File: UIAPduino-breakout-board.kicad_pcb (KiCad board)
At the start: 2 copper layers, 5 parts, among them J1 Conn_01x20_Pin, J2 Conn_01x20_Socket

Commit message: reload
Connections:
- J1 pad 7: GND -> Net-(J1-Pin_7)
- J2 pad 7: GND -> Net-(J1-Pin_7)
- U2 pad 18: Net-(J1-Pin_9) -> Net-(J1-Pin_8)
- U2 pad 22: Net-(J1-Pin_8) -> Net-(J1-Pin_7)
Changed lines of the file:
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@@
 	(net 18 "Net-(U1-TX)")
 	(net 19 "Net-(U1-RX)")
+	(net 20 "Net-(J1-Pin_7)")
 	(footprint "akizuki:FT234X"
 		(layer "F.Cu")
@@
 			(layers "*.Cu" "*.Mask")
 			(remove_unused_layers no)
-			(net 3 "GND")
+			(net 20 "Net-(J1-Pin_7)")
 			(pinfunction "Pin_7")
 			(pintype "passive")
@@
 			(layers "*.Cu" "*.Paste" "*.Mask")
 			(remove_unused_layers no)
-			(net 7 "Net-(J1-Pin_9)")
+			(net 2 "Net-(J1-Pin_8)")
 			(pinfunction "0/A1")
 			(pintype "bidirectional")
@@
 			(layers "*.Cu" "*.Paste" "*.Mask")
 			(remove_unused_layers no)
-			(net 2 "Net-(J1-Pin_8)")
+			(net 20 "Net-(J1-Pin_7)")
 			(pinfunction "~{RESET}")
 			(pintype "power_in")
@@
 			(layers "*.Cu" "*.Mask")
 			(remove_unused_layers no)
-			(net 3 "GND")
+			(net 20 "Net-(J1-Pin_7)")
 			(pinfunction "Pin_7")
 			(pintype "passive")

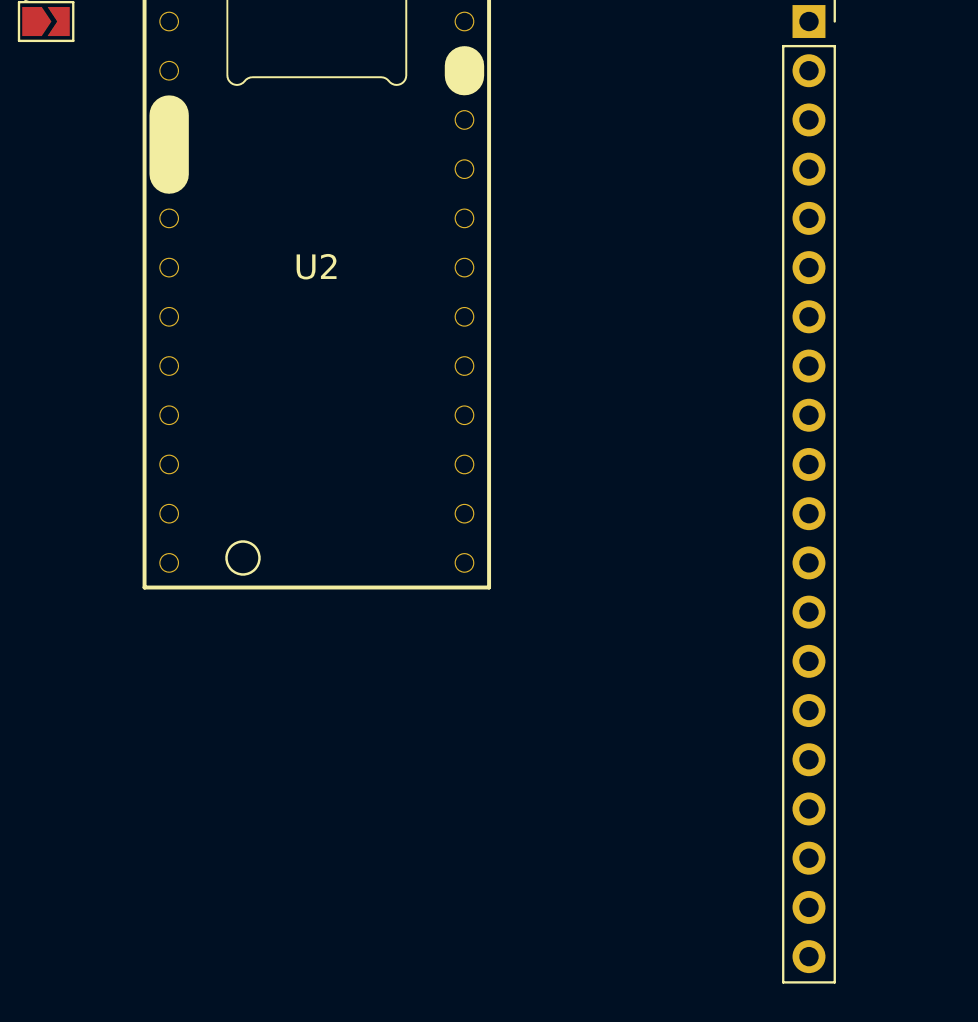
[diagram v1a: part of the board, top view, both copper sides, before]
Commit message: 信号線を配線
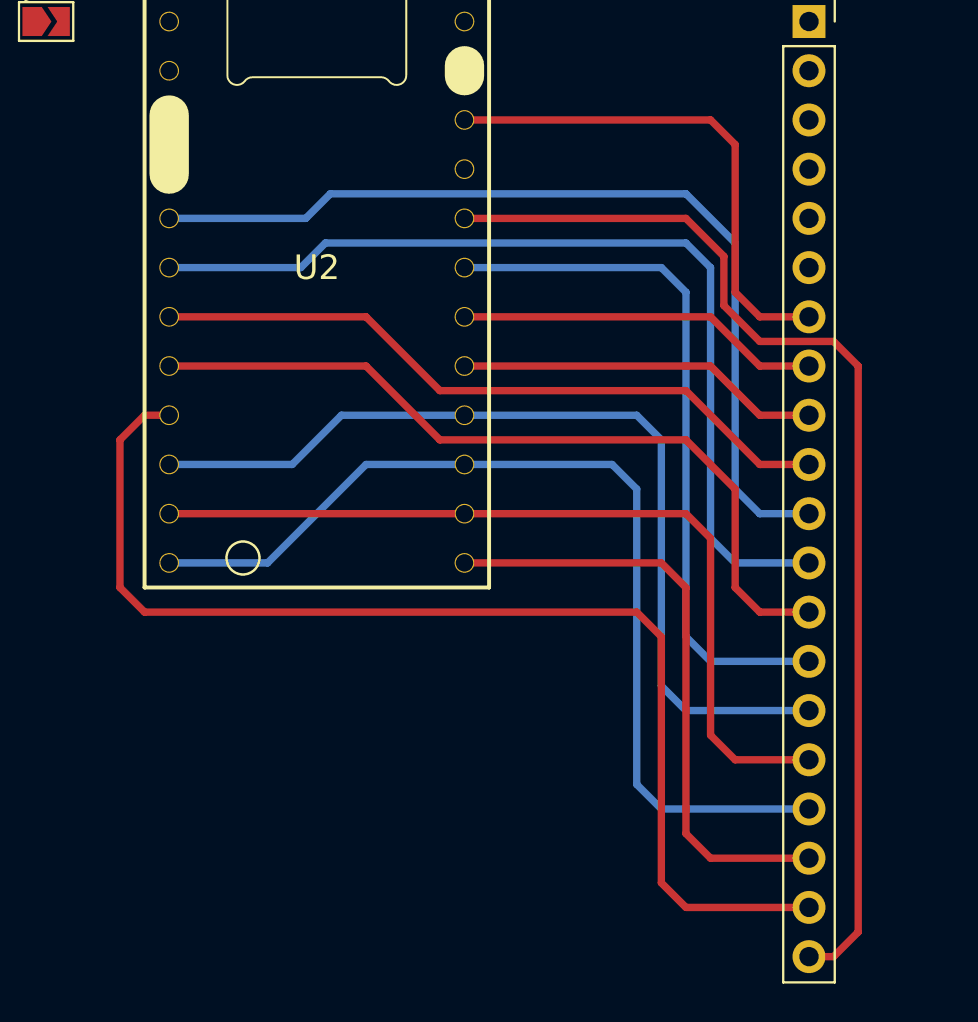
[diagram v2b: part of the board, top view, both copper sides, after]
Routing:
- net Net-(J1-Pin_19): track 0.00 -> 60.5 mm
- net Net-(J1-Pin_20): track 0.00 -> 57.2 mm
- net Net-(J1-Pin_17): track 0.00 -> 51.4 mm
- net Net-(J1-Pin_12): track 0.00 -> 48.6 mm
- net Net-(J1-Pin_15): track 0.00 -> 47.8 mm
- net Net-(J1-Pin_11): track 0.00 -> 47.8 mm
- net Net-(J1-Pin_16): track 0.00 -> 44.2 mm
- net Net-(J1-Pin_13): track 0.00 -> 41.3 mm
- net Net-(J1-Pin_14): track 0.00 -> 36.6 mm
- net Net-(J1-Pin_10): track 0.00 -> 36.2 mm
- net Net-(J1-Pin_18): track 0.00 -> 31.5 mm
- net Net-(J1-Pin_7): track 0.00 -> 26.5 mm
- net Net-(J1-Pin_8): track 0.00 -> 18.8 mm
- net Net-(J1-Pin_9): track 0.00 -> 18.8 mm

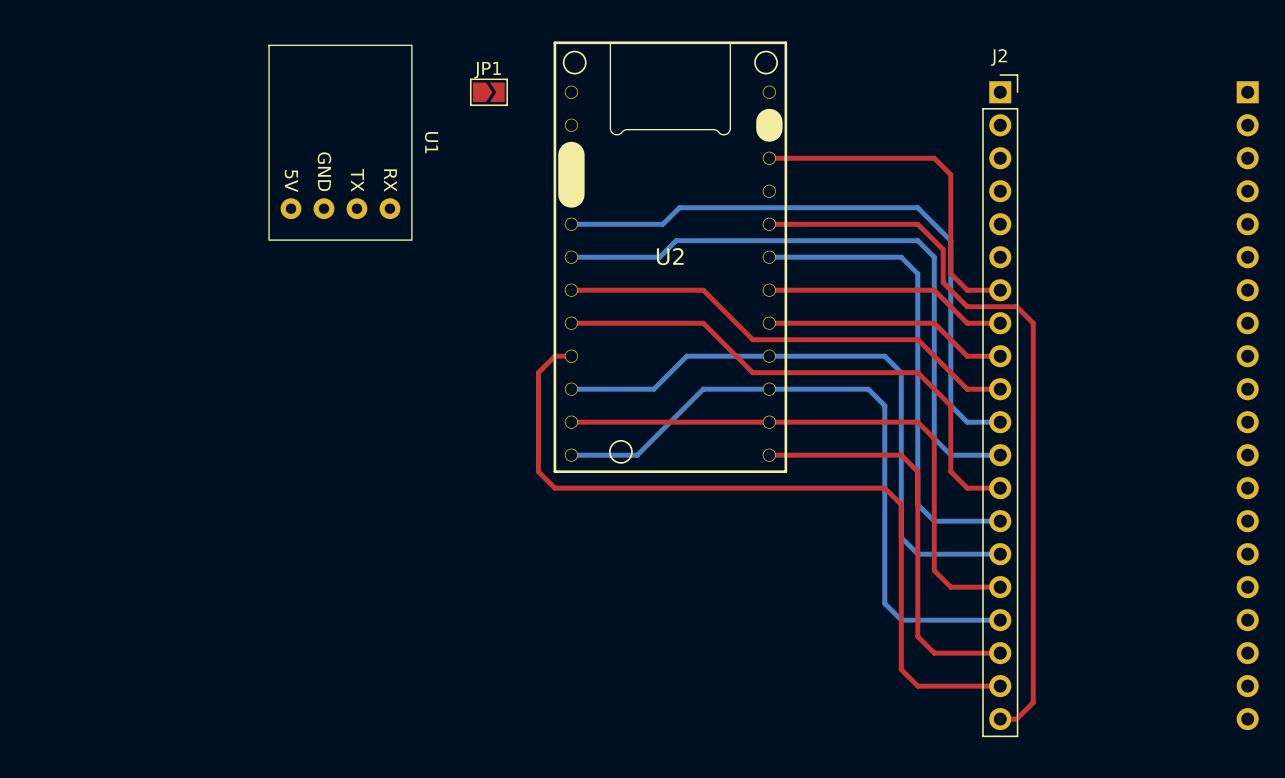
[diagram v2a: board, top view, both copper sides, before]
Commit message: 電源配置を変更
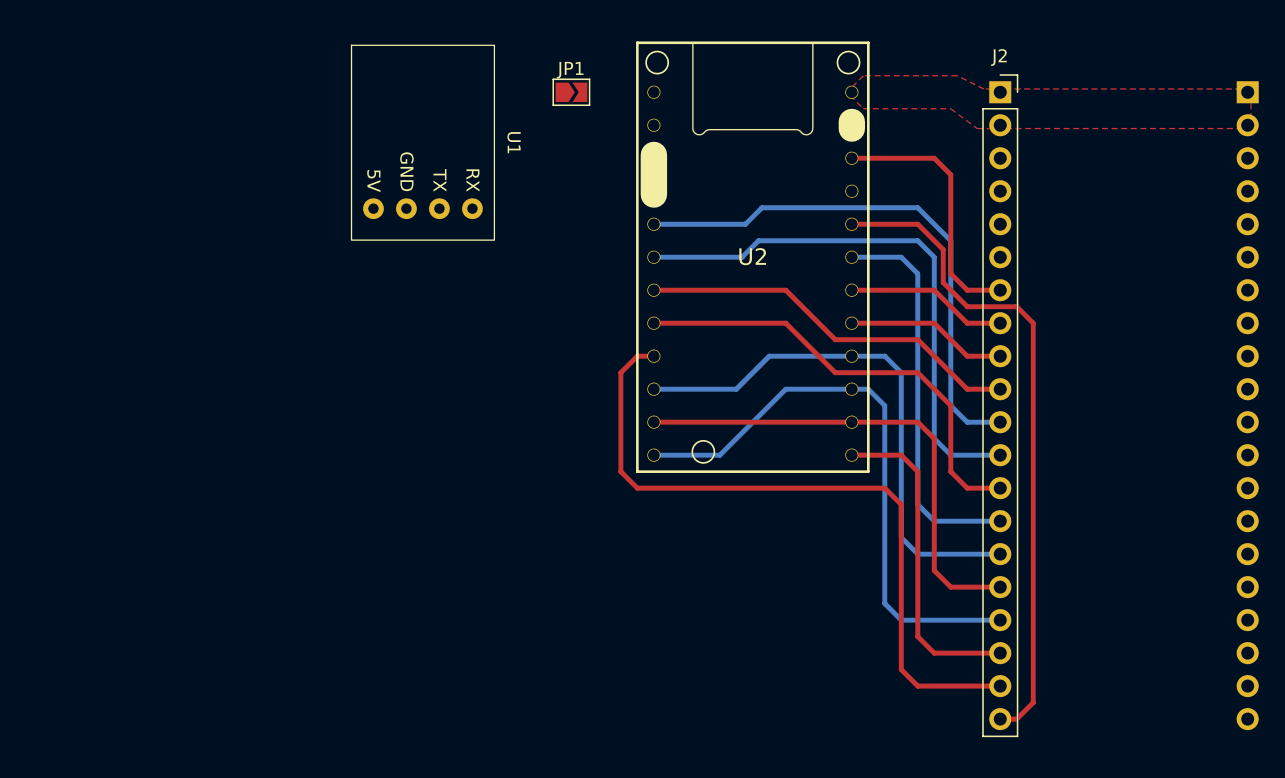
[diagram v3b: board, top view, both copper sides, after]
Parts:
- moved JP1 6.35 mm to (138.4, 67.3)
- moved U1 6.35 mm to (127.0, 63.6)
- moved U2 6.35 mm to (152.4, 80.0)
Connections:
- J1 pad 3: +3.3V -> GND
- J1 pad 4: +3.3V -> GND
- J1 pad 5: GND -> +3.3V
- J1 pad 6: GND -> +3.3V
- J2 pad 3: +3.3V -> GND
- J2 pad 4: +3.3V -> GND
- J2 pad 5: GND -> +3.3V
- J2 pad 6: GND -> +3.3V
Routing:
- net Net-(J1-Pin_19): track 60.5 -> 54.2 mm
- net Net-(J1-Pin_9): track 18.8 -> 12.5 mm
- net Net-(J1-Pin_8): track 18.8 -> 12.5 mm
- net Net-(J1-Pin_7): track 26.5 -> 20.1 mm
- net Net-(J1-Pin_20): track 57.2 -> 50.9 mm
- net Net-(J1-Pin_18): track 31.5 -> 25.2 mm
- net Net-(J1-Pin_14): track 36.6 -> 30.3 mm
- net Net-(J1-Pin_12): track 48.6 -> 42.2 mm
- net Net-(J1-Pin_16): track 44.2 -> 37.9 mm
- net Net-(J1-Pin_13): track 41.3 -> 34.9 mm
- net Net-(J1-Pin_11): track 47.8 -> 41.5 mm
- net Net-(J1-Pin_10): track 36.2 -> 29.8 mm
- net Net-(J1-Pin_17): track 51.4 -> 45.1 mm
- net Net-(J1-Pin_15): track 47.8 -> 41.5 mm
- added copper zone on F.Cu, net +5V

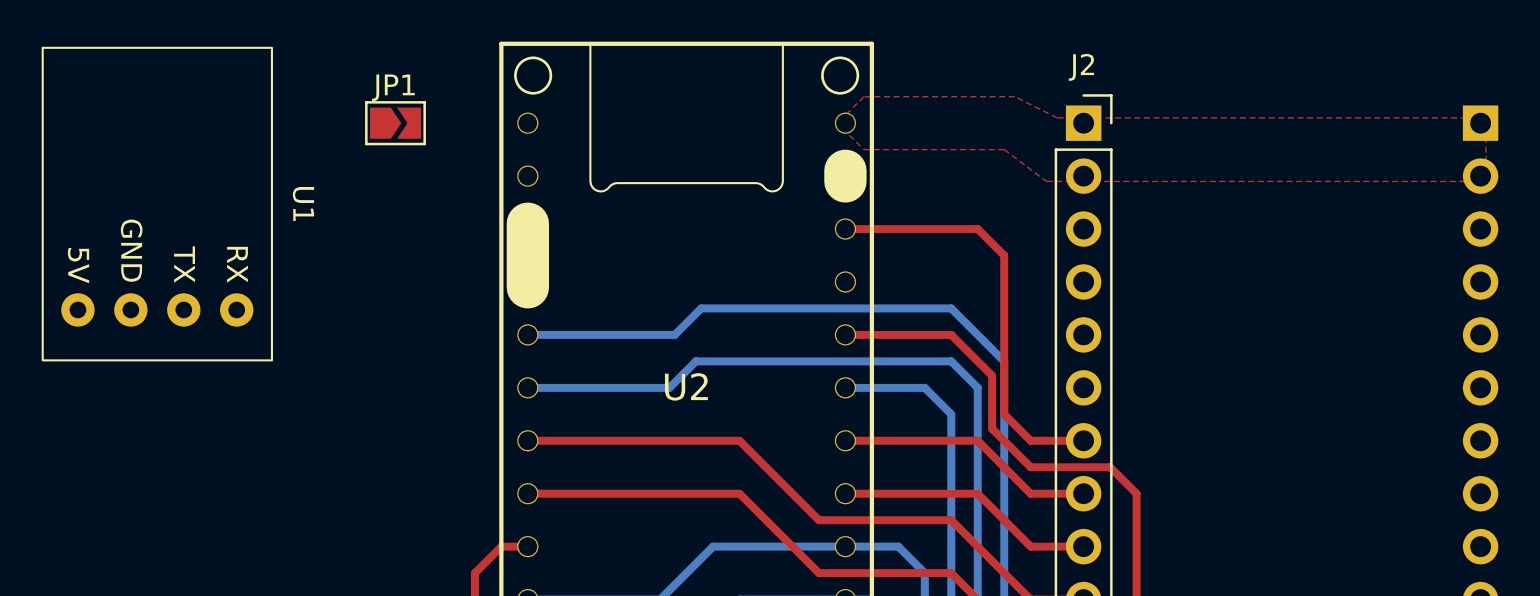
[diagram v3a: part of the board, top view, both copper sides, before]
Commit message: 配線をいい感じに
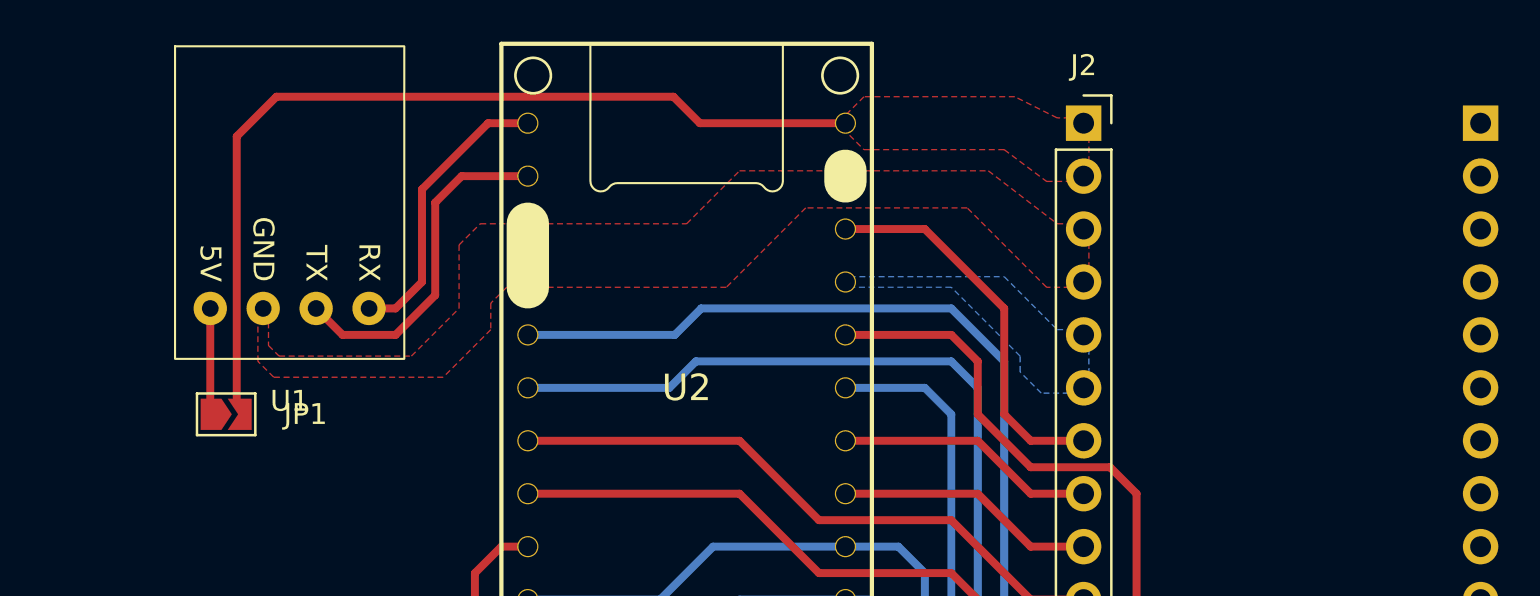
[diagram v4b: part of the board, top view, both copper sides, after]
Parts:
- moved JP1 16.2 mm to (130.3, 81.3)
- moved U1 6.35 mm to (133.3, 63.5)
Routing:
- net +5V: track 0.00 -> 43.7 mm
- net Net-(U1-TX): track 0.00 -> 16.4 mm
- net Net-(U1-RX): track 0.00 -> 13.9 mm
- net Net-(JP1-A): track 0.00 -> 5.08 mm
- net Net-(J1-Pin_7): track 20.1 -> 18.6 mm
- added copper zone on B.Cu, net +3.3V
- added copper zone on F.Cu, net GND
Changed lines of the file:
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@@
 	(footprint "akizuki:FT234X"
 		(layer "F.Cu")
-		(at 127 63.5725)
+		(at 133.35 63.5)
 		(property "Reference" "U1"
-			(at 6.985 7.62 -90)
+			(at 0 17.145 0)
 			(unlocked yes)
 			(layer "F.SilkS")
@@
 			(pinfunction "5V")
 			(pintype "power_out")
+			(thermal_bridge_angle 0)
 		)
 		(pad "2" thru_hole circle
@@
 			(pinfunction "GND")
 			(pintype "power_in")
+			(thermal_bridge_angle 0)
 		)
 		(pad "3" thru_hole circle
@@
 	(footprint "Jumper:SolderJumper-2_P1.3mm_Open_TrianglePad1.0x1.5mm"
 		(layer "F.Cu")
-		(at 138.43 67.31)
+		(at 130.302 81.28)
 		(descr "SMD Solder Jumper, 1x1.5mm Triangular Pads, 0.3mm gap, open")
 		(tags "solder jumper open")
 		(property "Reference" "JP1"
-			(at 0 -1.8 0)
+			(at 3.81 0 180)
 			(layer "F.SilkS")
 			(effects
@@
 		)
 		(property "Value" "Jumper_2_Open"
-			(at 0 1.9 0)
+			(at 0 1.9 360)
 			(layer "F.Fab")
 			(effects
@@
 			(pinfunction "GND")
 			(pintype "power_in")
+			(thermal_bridge_angle 0)
 		)
 		(pad "4" thru_hole circle
@@
 			(pinfunction "GND")
 			(pintype "power_in")
+			(thermal_bridge_angle 0)
 		)
 		(pad "5" thru_hole circle
@@
 			(pinfunction "3V3")
 			(pintype "power_in")
+			(thermal_bridge_angle 0)
 		)
 		(pad "22" thru_hole circle
@@
 			(pinfunction "GND")
 			(pintype "power_in")
+			(thermal_bridge_angle 0)
 		)
 		(pad "24" thru_hole circle
@@
 	)
 	(segment
+		(start 130.81 80.772)
+		(end 130.81 67.945)
+		(width 0.381)
+		(layer "F.Cu")
+		(net 1)
+	)
+	(segment
+		(start 153.035 67.31)
+		(end 160.02 67.31)
+		(width 0.381)
+		(layer "F.Cu")
+		(net 1)
+	)
+	(segment
+		(start 130.81 67.945)
+		(end 132.715 66.04)
+		(width 0.381)
+		(layer "F.Cu")
+		(net 1)
+	)
+	(segment
+		(start 131.064 81.026)
+		(end 130.81 80.772)
+		(width 0.381)
+		(layer "F.Cu")
+		(net 1)
+	)
+	(segment
+		(start 151.765 66.04)
+		(end 153.035 67.31)
+		(width 0.381)
+		(layer "F.Cu")
+		(net 1)
+	)
+	(segment
+		(start 132.715 66.04)
+		(end 151.765 66.04)
+		(width 0.381)
+		(layer "F.Cu")
+		(net 1)
+	)
+	(segment
 		(start 168.91 85.09)
 		(end 166.37 82.55)
@@
 	)
 	(segment
-		(start 172.72 83.82)
-		(end 173.99 85.09)
+		(start 166.37 78.74)
+		(end 166.37 81.28)
 		(width 0.381)
 		(layer "F.Cu")
@@
 	)
 	(segment
-		(start 167.059 81.969)
-		(end 168.91 83.82)
+		(start 165.1 77.47)
+		(end 166.37 78.74)
 		(width 0.381)
 		(layer "F.Cu")
@@
 	)
 	(segment
-		(start 165.1 77.47)
-		(end 160.02 77.47)
+		(start 173.99 114.3)
+		(end 172.72 115.57)
 		(width 0.381)
 		(layer "F.Cu")
@@
 	)
 	(segment
-		(start 173.99 85.09)
-		(end 173.99 114.3)
+		(start 172.72 83.82)
+		(end 173.99 85.09)
 		(width 0.381)
 		(layer "F.Cu")
@@
 	)
 	(segment
-		(start 167.059 79.429)
-		(end 167.059 81.969)
+		(start 166.37 81.28)
+		(end 168.91 83.82)
 		(width 0.381)
 		(layer "F.Cu")
@@
 	)
 	(segment
-		(start 165.1 77.47)
-		(end 167.059 79.429)
+		(start 172.72 115.57)
+		(end 171.45 115.57)
 		(width 0.381)
 		(layer "F.Cu")
@@
 	)
 	(segment
-		(start 173.99 114.3)
-		(end 172.72 115.57)
+		(start 168.91 83.82)
+		(end 172.72 83.82)
 		(width 0.381)
 		(layer "F.Cu")
@@
 	)
 	(segment
-		(start 172.72 115.57)
-		(end 171.45 115.57)
+		(start 160.02 77.47)
+		(end 165.1 77.47)
 		(width 0.381)
 		(layer "F.Cu")
@@
 	)
 	(segment
-		(start 168.91 83.82)
-		(end 172.72 83.82)
+		(start 173.99 85.09)
+		(end 173.99 114.3)
 		(width 0.381)
 		(layer "F.Cu")
@@
 	)
 	(segment
-		(start 166.37 72.39)
-		(end 160.02 72.39)
+		(start 129.54 81.28)
+		(end 129.54 76.2)
 		(width 0.381)
 		(layer "F.Cu")
-		(net 20)
+		(net 17)
 	)
 	(segment
-		(start 168.91 82.55)
-		(end 167.64 81.28)
+		(start 138.43 77.47)
+		(end 140.335 75.565)
 		(width 0.381)
 		(layer "F.Cu")
-		(net 20)
+		(net 18)
+	)
+	(segment
+		(start 135.89 77.47)
+		(end 138.43 77.47)
+		(width 0.381)
+		(layer "F.Cu")
+		(net 18)
+	)
+	(segment
+		(start 134.62 76.2)
+		(end 135.89 77.47)
+		(width 0.381)
+		(layer "F.Cu")
+		(net 18)
+	)
+	(segment
+		(start 140.335 75.565)
+		(end 140.335 71.12)
+		(width 0.381)
+		(layer "F.Cu")
+		(net 18)
+	)
+	(segment
+		(start 141.605 69.85)
+		(end 144.78 69.85)
+		(width 0.381)
+		(layer "F.Cu")
+		(net 18)
+	)
+	(segment
+		(start 140.335 71.12)
+		(end 141.605 69.85)
+		(width 0.381)
+		(layer "F.Cu")
+		(net 18)
+	)
+	(segment
+		(start 142.875 67.31)
+		(end 139.7 70.485)
+		(width 0.381)
+		(layer "F.Cu")
+		(net 19)
+	)
+	(segment
+		(start 139.7 70.485)
+		(end 139.7 74.93)
+		(width 0.381)
+		(layer "F.Cu")
+		(net 19)
+	)
+	(segment
+		(start 138.43 76.2)
+		(end 137.16 76.2)
+		(width 0.381)
+		(layer "F.Cu")
+		(net 19)
+	)
+	(segment
+		(start 144.78 67.31)
+		(end 142.875 67.31)
+		(width 0.381)
+		(layer "F.Cu")
+		(net 19)
+	)
+	(segment
+		(start 139.7 74.93)
+		(end 138.43 76.2)
+		(width 0.381)
+		(layer "F.Cu")
+		(net 19)
 	)
 	(segment
@@
 	)
 	(segment
+		(start 163.83 72.39)
+		(end 160.02 72.39)
+		(width 0.381)
+		(layer "F.Cu")
+		(net 20)
+	)
+	(segment
 		(start 167.64 81.28)
-		(end 167.64 73.66)
+		(end 167.64 76.2)
 		(width 0.381)
 		(layer "F.Cu")
@@
 	)
 	(segment
-		(start 167.64 73.66)
-		(end 166.37 72.39)
+		(start 167.64 76.2)
+		(end 163.83 72.39)
+		(width 0.381)
+		(layer "F.Cu")
+		(net 20)
+	)
+	(segment
+		(start 168.91 82.55)
+		(end 167.64 81.28)
 		(width 0.381)
 		(layer "F.Cu")
@@
 		(polygon
 			(pts
-				(xy 190.754 70.104) (xy 190.754 67.056) (xy 170.18 67.056) (xy 168.148 66.04) (xy 160.909 66.04)
+				(xy 171.704 70.104) (xy 171.704 67.056) (xy 170.18 67.056) (xy 168.148 66.04) (xy 160.909 66.04)
 				(xy 159.893 67.056) (xy 159.893 67.564) (xy 160.909 68.58) (xy 167.64 68.58) (xy 169.672 70.104)
 			)
 		)
+	)
+	(zone
+		(net 3)
+		(net_name "GND")
+		(layer "F.Cu")
+		(hatch edge 0.5)
+		(priority 1)
+		(connect_pads
+			(clearance 0.5)
+		)
+		(min_thickness 0.25)
+		(filled_areas_thickness no)
+		(fill yes
+			(thermal_gap 0.5)
+			(thermal_bridge_width 0.5)
+		)
+		(polygon
+			(pts
+				(xy 152.4 72.136) (xy 154.94 69.596) (xy 166.878 69.596) (xy 170.18 72.136) (xy 171.704 72.136)
+				(xy 171.704 75.184) (xy 169.672 75.184) (xy 165.862 71.374) (xy 158.115 71.374) (xy 154.305 75.184)
+				(xy 143.764 75.184) (xy 143.002 75.946) (xy 143.002 77.216) (xy 140.716 79.502) (xy 132.588 79.502)
+				(xy 131.826 78.74) (xy 131.826 75.946) (xy 132.334 75.946) (xy 132.334 77.978) (xy 132.842 78.486)
+				(xy 139.192 78.486) (xy 141.478 76.2) (xy 141.478 73.152) (xy 142.494 72.136)
+			)
+		)
+	)
+	(zone
+		(net 11)
+		(net_name "+3.3V")
+		(layer "B.Cu")
+		(hatch edge 0.5)
+		(priority 2)
+		(connect_pads
+			(clearance 0.5)
+		)
+		(min_thickness 0.25)
+		(filled_areas_thickness no)
+		(fill yes
+			(thermal_gap 0.5)
+			(thermal_bridge_width 0.5)
+		)
+		(polygon
+			(pts
+				(xy 171.704 77.216) (xy 171.704 80.264) (xy 171.196 80.264) (xy 169.418 80.264) (xy 168.402 79.248)
+				(xy 168.402 78.486) (xy 165.1 75.184) (xy 159.766 75.184) (xy 159.766 74.676) (xy 167.64 74.676)
+				(xy 170.18 77.216)
+			)
+		)
